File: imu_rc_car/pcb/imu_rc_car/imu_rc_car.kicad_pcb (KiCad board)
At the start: 2 copper layers, 100 x 82.3 mm, 33 parts, among them J1 LiPo Battery, J2 Left Terminal, J3 Right Terminal, J4 Prox Sensor FS, J5 Prox Sensor LS, J6 Prox Sensor RS, J7 Prox Sensor BS, J8 Encoder F, J9 Encoder B, Q1 IRLML6344TRPBF, Q2 DMP3160L-7, Q3 IRLZ34N, SW1 SW_Nidec_CAS-120A1, U1 ESP32-S3-DevKitC, U3 AMS1117-3.3, U6 DRV8833PWP, U7 DRV8833PWP

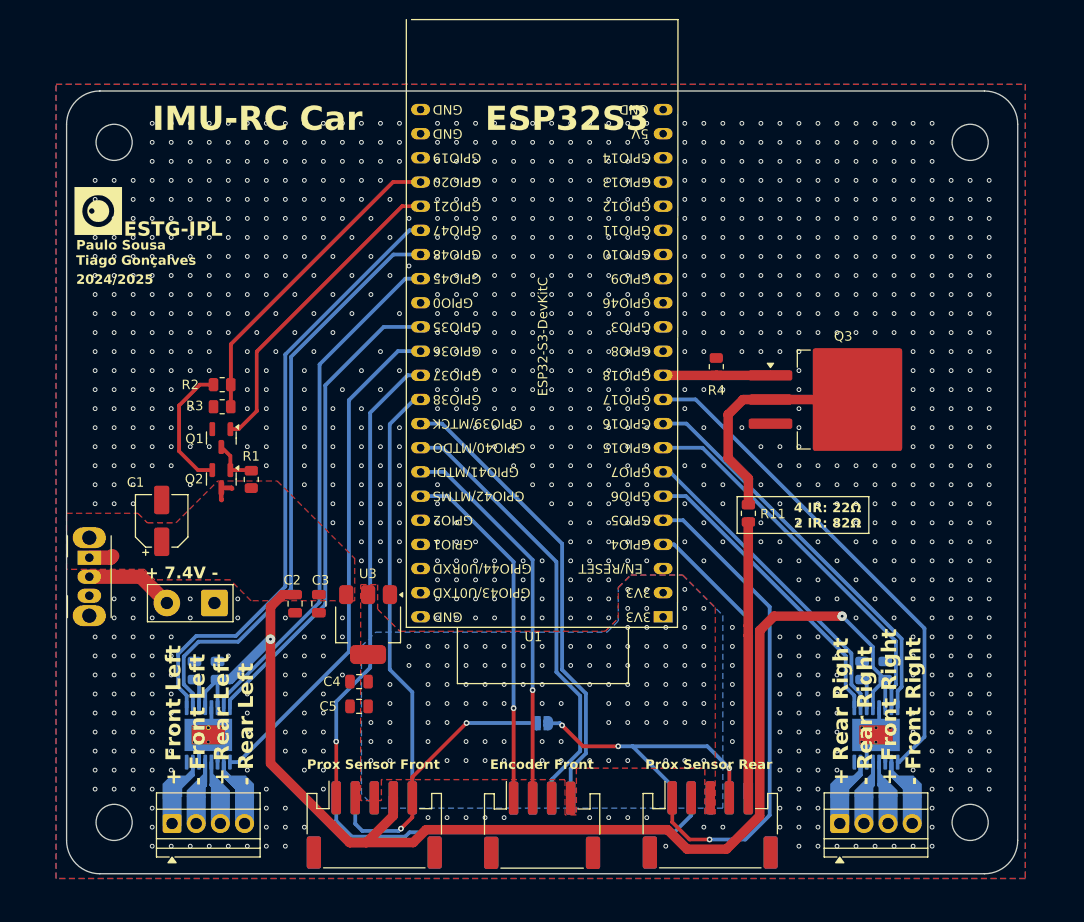
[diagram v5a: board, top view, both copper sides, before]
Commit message: commit #32
costs table 4
first revision of imu rc car pcb
imu rc encoders final version v1.0.0 (ordered)
imu rc prox sensors final version v1.0.0 (ordered)
minor resistors tolerance changes in hand unit
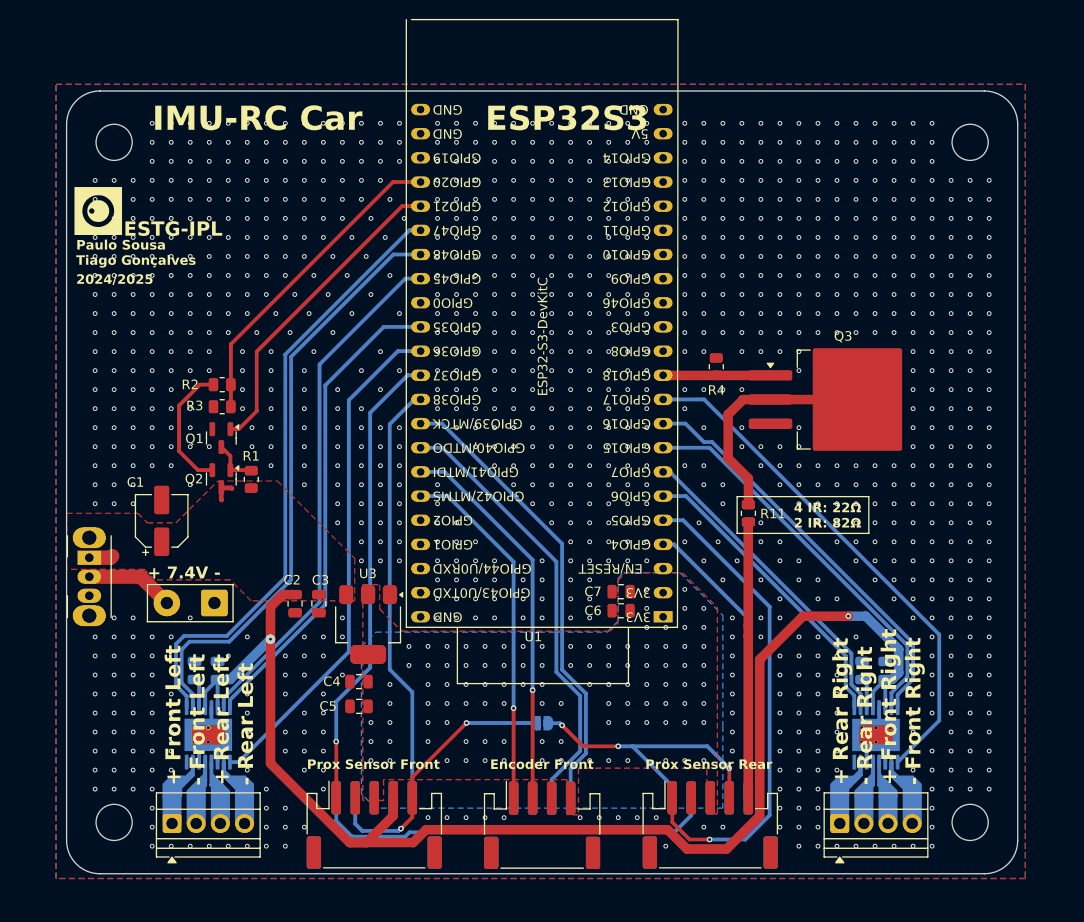
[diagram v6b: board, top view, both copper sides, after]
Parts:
- added C6: 10uF, Capacitor_SMD:C_0805_2012Metric, F.Cu at (153.3, 109.2)
- added C7: 100nF, Capacitor_SMD:C_0805_2012Metric, F.Cu at (153.3, 107.2)
- R11: value 10 -> 22 (1%)
- R2: value 51k -> 51k (1%)
- R3: value 33k -> 33k (1%)
- renumbered C8 to C10, C9 to C11, C6 to C8, C7 to C9
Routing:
- net STBYB: track 52.8 -> 54.5 mm
- net AIN4: track 40.1 -> 41.5 mm
- net AIN3: track 41.9 -> 43.3 mm
- net +7V4: track 147.4 -> 148.7 mm
- net GND: vias 1120 -> 1117
- net +3V3: vias 105 -> 102

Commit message: commit #33
minor changes in car pcb for plot files
fixed bottom holes position in prox sensor case
fixed supports and holes position in hand unit for the oled screen
increased length and width of internal area in hand unit for more pcb play
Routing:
- net GND: vias 1117 -> 1110

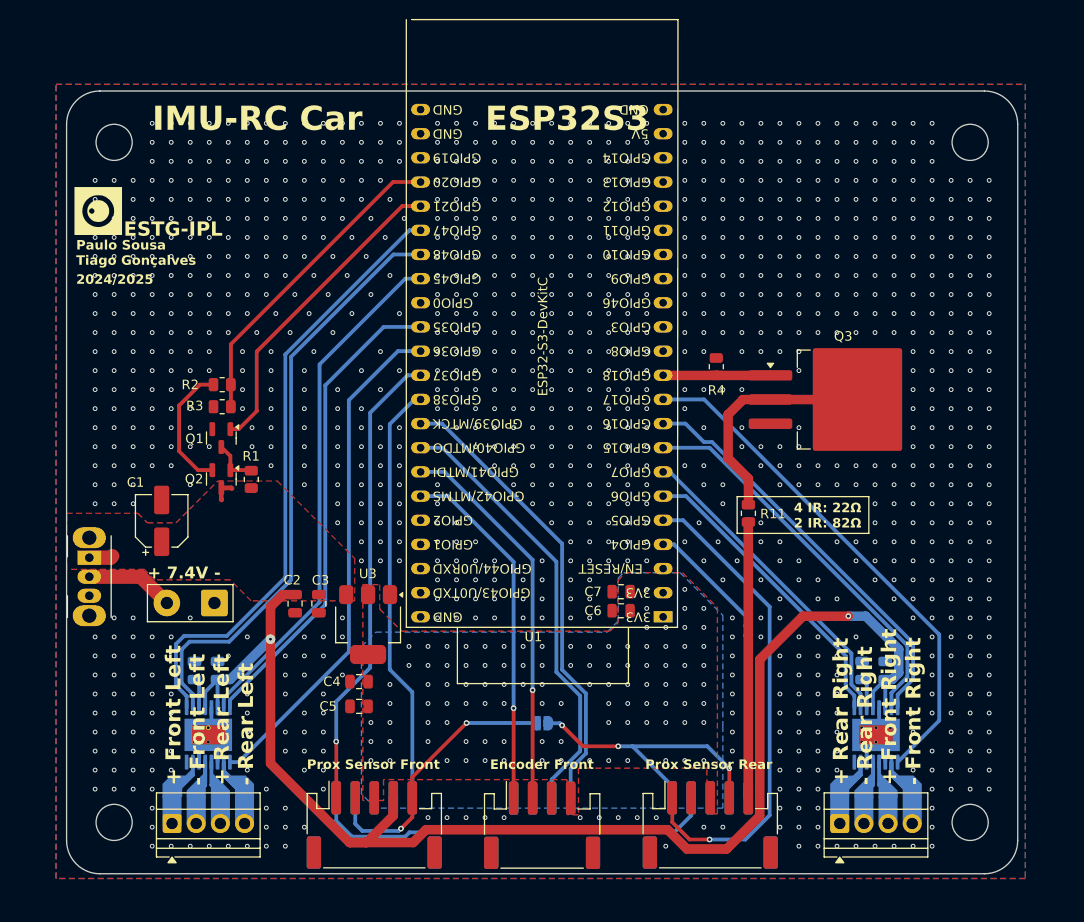
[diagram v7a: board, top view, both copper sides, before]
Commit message: commit #34
pcb hand unit v1.1.0:
chaged RGB led footprint to better fit
switch drain with source in Q5 MOSFET (battery reader)

pcb car v1.1.0:
removed power planes, added traces only
switch drain with source in Q1 MOSFET (battery reader)
changed LDO position

code:
changed esp32 devkit to esp32s3 devkit
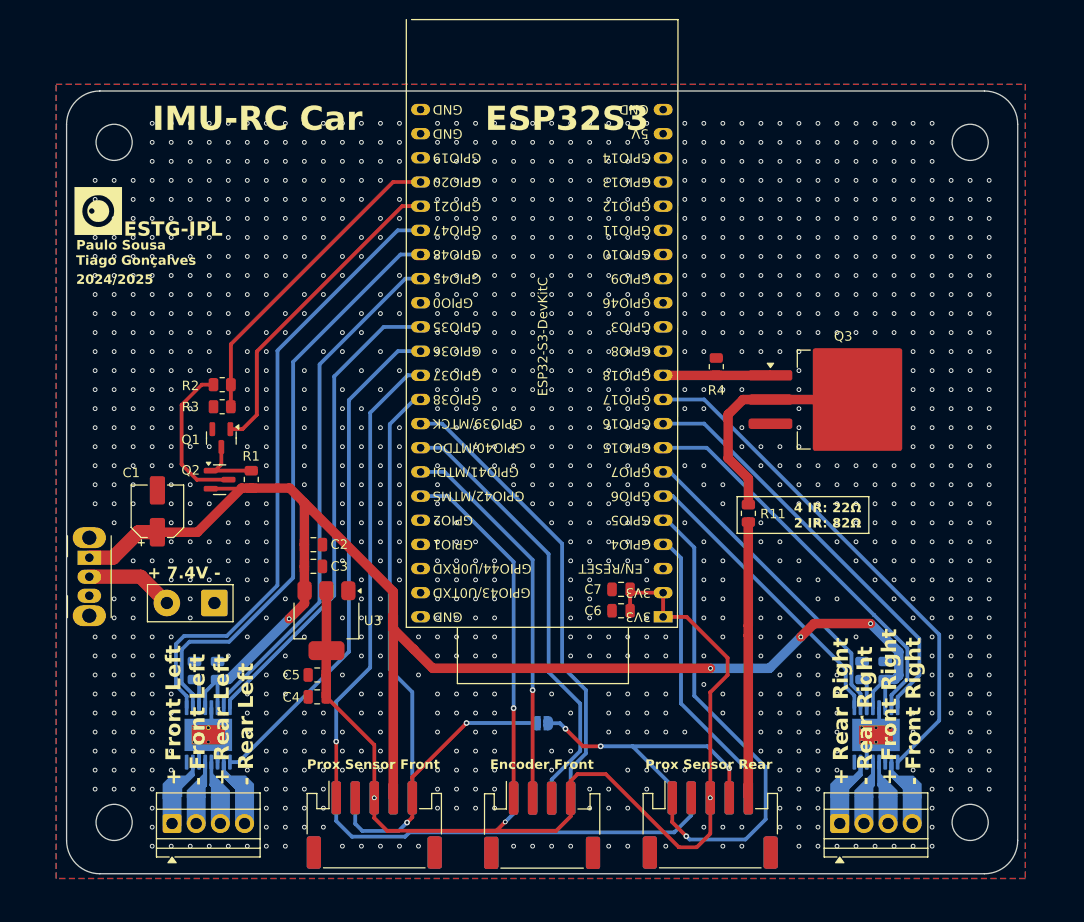
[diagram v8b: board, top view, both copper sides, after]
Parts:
- moved C2 6.50 mm to (121.0, 102.3), turned to 0 degrees
- moved C5 5.50 mm to (121.3, 116.0)
- moved C4 4.68 mm to (121.3, 118.3)
- moved U3 4.40 mm to (122.3, 110.3)
- moved C3 3.97 mm to (121.0, 104.6), turned to 0 degrees
- moved C1 1.11 mm to (104.5, 98.8)
- moved C7 0.25 mm to (153.3, 107.0)
- moved Q2 0.20 mm to (111.1, 95.5), turned to 0 degrees
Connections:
- Q2 pad 2: Net-(Q2-S) -> +7V4
- Q2 pad 3: +7V4 -> Net-(Q2-D)
- R2 pad 1: Net-(Q2-S) -> Net-(Q2-D)
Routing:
- net +3V3: track 0.00 -> 111.9 mm, vias 102 -> 3
- net +7V4: track 148.7 -> 165.0 mm, vias 2 -> 4
- net Net-(Q2-D): track 0.00 -> 16.1 mm
- net Net-(Q2-S): track 13.6 -> 0.00 mm
- net Net-(Q1-D): track 5.05 -> 7.50 mm
- net PRX_BS: track 51.5 -> 50.2 mm
- net AIN3: track 43.3 -> 44.5 mm
- net BIN3: track 32.0 -> 31.2 mm
- net BIN1: track 64.6 -> 65.3 mm
- net GND: vias 1110 -> 1267
- removed copper zone on B.Cu, net +3V3
- removed copper zone on F.Cu, net +3V3
- removed copper zone on F.Cu, net +7V4
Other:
- board text added: "v1.1.0"
- board text removed: "v1.0.0"
